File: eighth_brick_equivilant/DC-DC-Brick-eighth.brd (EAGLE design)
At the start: 31.1 x 77.5 mm, 20 parts

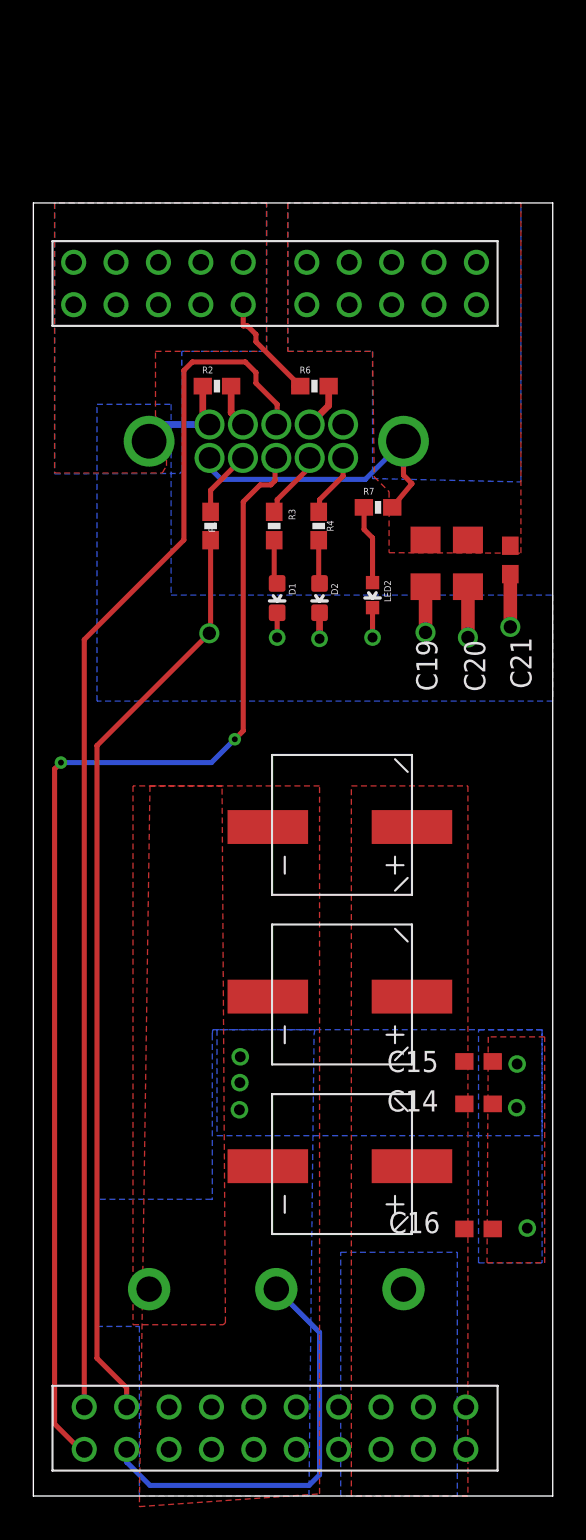
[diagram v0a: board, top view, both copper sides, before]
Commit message: Added mounting holes to circuit board
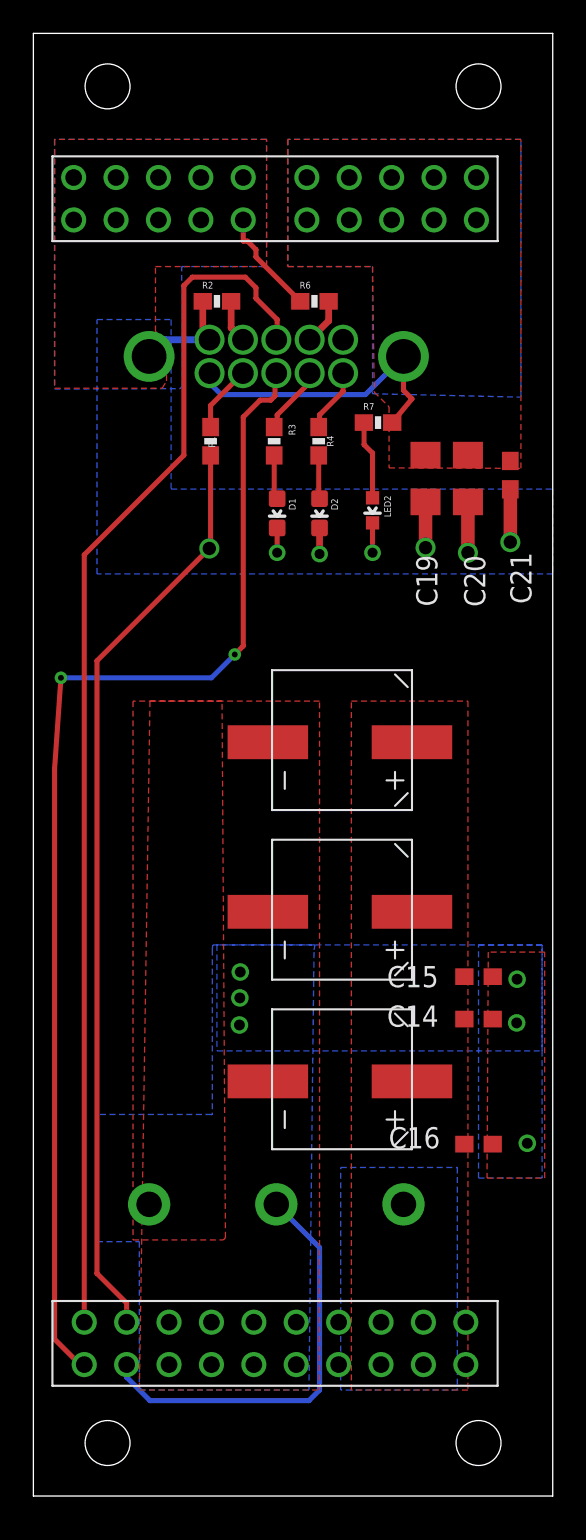
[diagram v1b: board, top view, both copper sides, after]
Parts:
- moved C21 5.08 mm to (28.6, 61.2)
- moved C22V5 5.08 mm to (14.3, 39.3)
- moved D1 5.08 mm to (14.6, 58.9)
- moved D2 5.08 mm to (17.1, 58.9)
- moved U$4 5.08 mm to (6.22, 59.9)
- moved C16 5.08 mm to (26.7, 21.1)
- moved C14 5.08 mm to (26.7, 28.6)
- moved C15 5.08 mm to (26.7, 31.1)
- moved C19 5.08 mm to (23.5, 61.0)
- moved C20 5.08 mm to (26.0, 61.0)
- moved C22V1 5.08 mm to (14.3, 49.5)
- moved C22V6 5.08 mm to (14.3, 29.2)
- moved LED2 5.08 mm to (20.3, 59.1)
- moved R1 5.08 mm to (10.6, 63.2)
- moved R2 5.08 mm to (11.0, 71.6)
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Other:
- board size 31.1 x 77.5 mm -> 31.1 x 87.6 mm

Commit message: Made the eighth brick thinner
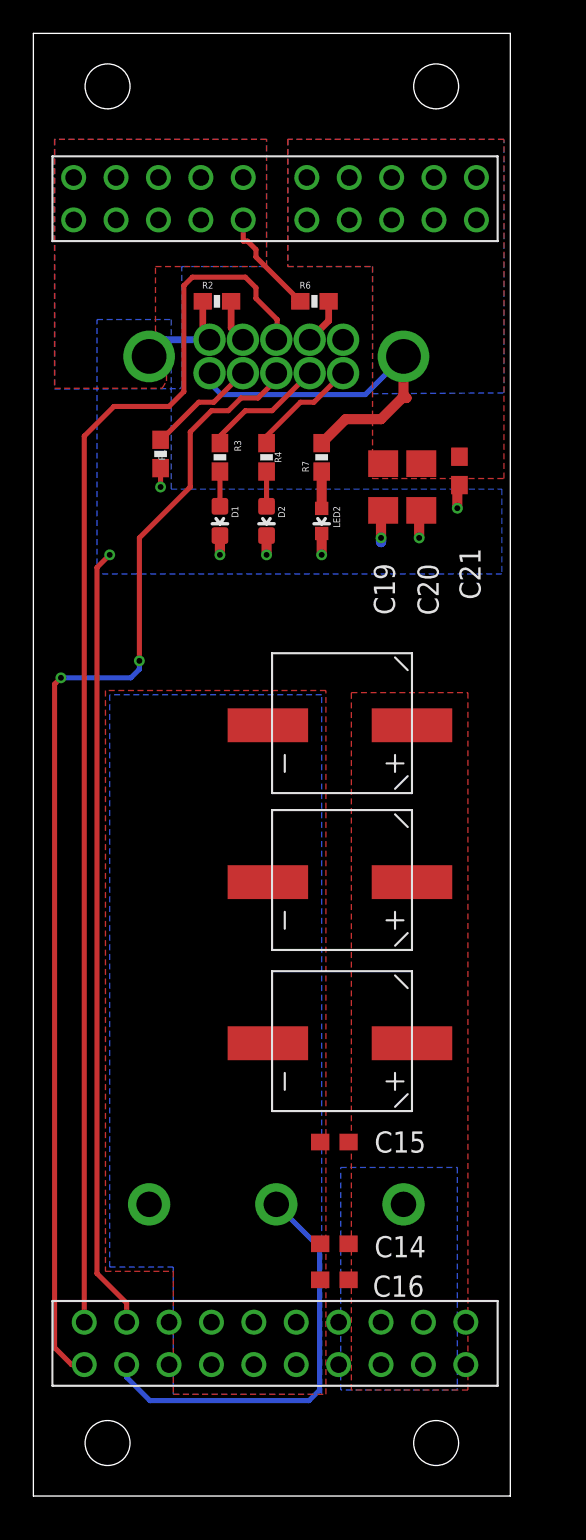
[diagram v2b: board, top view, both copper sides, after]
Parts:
- moved C14 16.0 mm to (18.0, 15.1), turned to 180 degrees
- moved C15 13.1 mm to (18.0, 21.2), turned to 180 degrees
- moved C16 11.9 mm to (18.0, 13.0), turned to 180 degrees
- moved R7 3.97 mm to (17.3, 62.2), turned to 90 degrees
- moved D1 3.46 mm to (11.2, 58.4)
- moved R3 3.39 mm to (11.2, 62.2)
- moved R4 3.27 mm to (14.0, 62.2)
- moved D2 3.21 mm to (14.0, 58.4)
- moved LED2 3.11 mm to (17.3, 58.4)
- moved R1 3.09 mm to (7.62, 62.4)
- moved C21 3.06 mm to (25.5, 61.4)
- moved C20 2.84 mm to (23.2, 60.5)
- moved C19 2.59 mm to (21.0, 60.5)
- moved C22V6 2.29 mm to (14.3, 31.4)
- moved C22V5 1.78 mm to (14.3, 41.1)
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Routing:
- net GND: track 82.6 -> 70.5 mm, vias 7 -> 8
- net V+: track 18.0 -> 22.2 mm
- net N$7: track 4.11 -> 7.36 mm
- net N$6: track 3.83 -> 6.57 mm
- net N$2: track 4.03 -> 6.59 mm
- net N$12: track 4.72 -> 2.21 mm
- net SDA: track 73.0 -> 75.0 mm
- net SCL: track 71.3 -> 69.7 mm
- net N$4: track 2.66 -> 2.08 mm
- net N$5: track 2.61 -> 2.08 mm
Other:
- board size 31.1 x 87.6 mm -> 28.6 x 87.6 mm
